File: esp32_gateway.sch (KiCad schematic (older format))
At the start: 75 parts, among them J1 POWER Int, J10 IRF, J11 Conn_01x01_Female, J12 Conn_01x01_Female, J13 Conn_01x01_Female, J14 Conn_01x01_Female, J15 Conn_01x01_Female, J16 Conn_01x01_Female, J17 Conn_01x01_Female, J18 Conn_01x01_Female, J19 Conn_01x01_Female, J2 POWER Out, J20 CC2530_B, J21 CC2530_A, J22 Conn_01x01_Female, J23 Conn_01x01_Female, J3 Conn_01x01_Female, J4 Conn_01x01_Female, J5 Uart, J6 Boot, J7 SRX882, J8 STX882, J9 Conn_01x01_Female, Q1 DMP4051LK3, Q2 BC847, Q3 BSS138, Q4 2N7002, Q5 2N7002, SW1 Reset, U1 LM1117-3.3, U2 ESP32-S

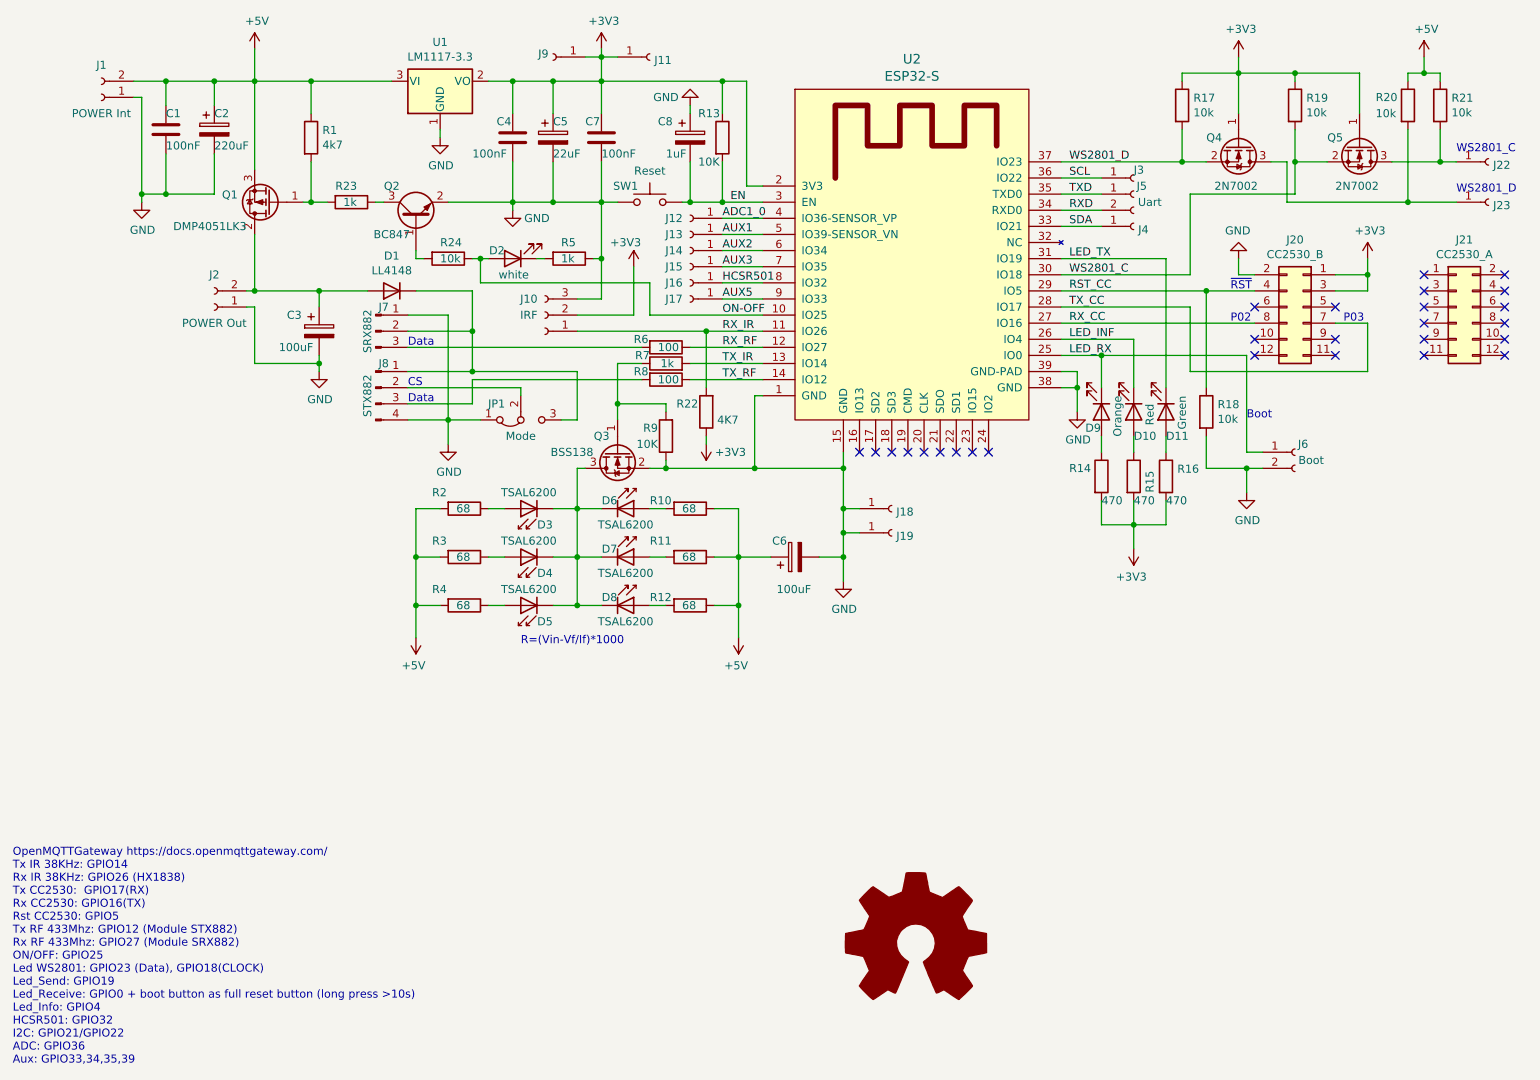
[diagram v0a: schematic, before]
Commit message: Fixed errors in RF modules connection
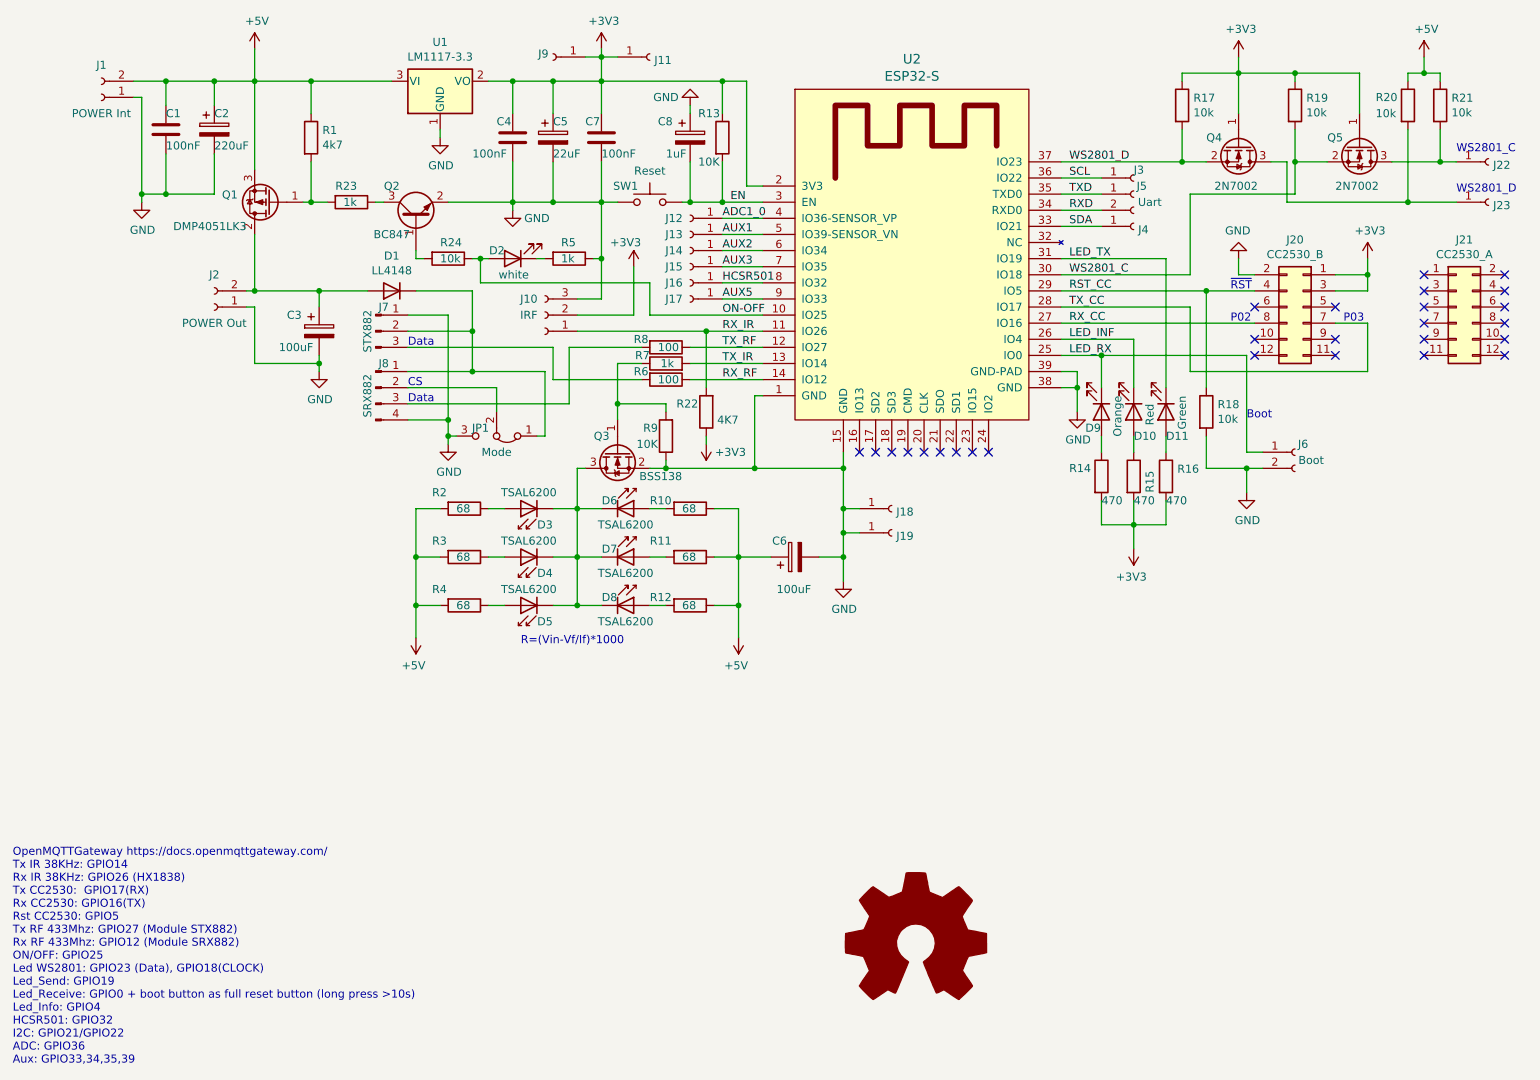
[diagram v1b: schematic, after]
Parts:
- J7: value SRX882 -> STX882
- J8: value STX882 -> SRX882
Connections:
- net GND: now also JP1.3 (B); no longer JP1.1 (A)
- net RX_RF: now also U2.14 (IO12); no longer U2.12 (IO27)
- net TX_RF: now also U2.12 (IO27); no longer U2.14 (IO12)
- net at D1.1 (K), J7.2 (Pin_2), J8.1 (Pin_1): now also JP1.1 (A); no longer JP1.3 (B)
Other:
- note added: "OpenMQTTGateway https://docs.openmqttgateway.com/\nTx IR 38KHz: GPIO14 \nRx IR 38KHz: GPIO26 (HX1838)\nTx CC2530: GPIO17(RX)\nRx CC2530: GPIO16(TX)\nRst CC2530: GPIO5\nTx RF 433Mhz: GPIO27 (Module STX882)\nRx RF 433Mhz: GPIO12 (Module SRX882)\nON/OFF: GPIO25\nLed WS2801: GPIO23 (Data), GPIO18(CLOCK)\nLed_Send: GPIO19\nLed_Receive: GPIO0 + boot button as full reset button (long press >10s)\nLed_In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"
- note removed: "OpenMQTTGateway https://docs.openmqttgateway.com/\nTx IR 38KHz: GPIO14 \nRx IR 38KHz: GPIO26 (HX1838)\nTx CC2530: GPIO17(RX)\nRx CC2530: GPIO16(TX)\nRst CC2530: GPIO5\nTx RF 433Mhz: GPIO12 (Module STX882)\nRx RF 433Mhz: GPIO27 (Module SRX882)\nON/OFF: GPIO25\nLed WS2801: GPIO23 (Data), GPIO18(CLOCK)\nLed_Send: GPIO19\nLed_Receive: GPIO0 + boot button as full reset button (long press >10s)\nLed_In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"
- moved on the sheet: JP1, R6, R8
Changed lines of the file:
@@
 Comment4 ""
 $EndDescr
-Text Notes 600  7750 0    50   ~ 0
-OpenMQTTGateway https://docs.openmqttgateway.com/\nTx IR 38KHz: GPIO14 \nRx IR 38KHz: GPIO26 (HX1838)\nTx CC2530:  GPIO17(RX)\nRx CC2530: GPIO16(TX)\nRst CC2530: GPIO5\nTx RF 433Mhz: GPIO12 (Module STX882)\nRx RF 433Mhz: GPIO27 (Module SRX882)\nON/OFF: GPIO25\nLed WS2801: GPIO23 (Data), GPIO18(CLOCK)\nLed_Send: GPIO19\nLed_Receive: GPIO0 + boot button as full reset button (long press >10s)\nLed_Info: GPIO4\nHCSR501: GPIO32\nI2C: GPIO21/GPIO22\nADC: GPIO36\nAux: GPIO33,34,35,39\n
 NoConn ~ 6450 3950
 NoConn ~ 6350 3950
@@
 RX_CC
 Text Label 5000 3500 0    50   ~ 0
-TX_RF
-Text Label 5000 3300 0    50   ~ 0
 RX_RF
 Text Label 7150 2750 0    50   ~ 0
@@
 $EndComp
 Wire Wire Line
-	3300 3750 3300 3900
+	3300 3750 3300 3850
 Connection ~ 3300 3750
 $Comp
@@
 Connection ~ 9450 2150
 $Comp
-L Device:R R8
-U 1 1 5FBA51B6
+L Device:R R6
+U 1 1 5FBBFD7C
 P 4650 3500
-F 0 "R8" V 4600 3300 50  0000 L CNN
+F 0 "R6" V 4600 3300 50  0000 L CNN
 F 1 "100" V 4650 3450 50  0000 L CNN
 F 2 "Resistor_SMD:R_0805_2012Metric" V 4580 3500 50  0001 C CNN
@@
 	0    1    1    0
 $EndComp
-Wire Wire Line
-	4800 3500 5250 3500
-$Comp
-L Device:R R6
-U 1 1 5FBBFD7C
-P 4650 3300
-F 0 "R6" V 4600 3100 50  0000 L CNN
-F 1 "100" V 4650 3250 50  0000 L CNN
-F 2 "Resistor_SMD:R_0805_2012Metric" V 4580 3300 50  0001 C CNN
-F 3 "~" H 4650 3300 50  0001 C CNN
-	1    4650 3300
-	0    1    1    0
-$EndComp
-Wire Wire Line
-	4800 3300 5250 3300
 Connection ~ 3450 3200
 Wire Wire Line
@@
 CS
 Wire Wire Line
-	3050 3550 3750 3550
-Wire Wire Line
 	3050 3200 3450 3200
 Wire Wire Line
@@
 P 2850 3550
 F 0 "J8" H 2900 3700 50  0000 C CNN
-F 1 "STX882" V 2800 3500 50  0000 C CNN
+F 1 "SRX882" V 2800 3500 50  0000 C CNN
 F 2 "Connector_PinHeader_2.54mm:PinHeader_1x04_P2.54mm_Vertical" H 2850 3550 50  0001 C CNN
 F 3 "~" H 2850 3550 50  0001 C CNN
@@
 	1    0    0    -1
 $EndComp
-Wire Wire Line
-	3050 3300 4500 3300
 $Comp
 L Connector:Conn_01x03_Female J10
@@
 	1    0    0    -1
 $EndComp
-$Comp
-L Jumper:Jumper_3_Bridged12 JP1
-U 1 1 5FA2F7B6
-P 3750 3750
-F 0 "JP1" H 3600 3650 50  0000 C CNN
-F 1 "Mode" H 3750 3850 50  0000 C CNN
-F 2 "Jumper:SolderJumper-3_P1.3mm_Bridged2Bar12_Pad1.0x1.5mm_NumberLabels" H 3750 3750 50  0001 C CNN
-F 3 "~" H 3750 3750 50  0001 C CNN
-	1    3750 3750
-	1    0    0    1
-$EndComp
-Wire Wire Line
-	3500 3750 3300 3750
-Wire Wire Line
-	3750 3600 3750 3550
-Wire Wire Line
-	3450 3450 4100 3450
+Wire Wire Line
+	3450 3450 3900 3450
 Connection ~ 3450 3450
 $Comp
@@
 P 2850 3200
 F 0 "J7" H 2900 3350 50  0000 C CNN
-F 1 "SRX882" V 2800 3200 50  0000 C CNN
+F 1 "STX882" V 2800 3200 50  0000 C CNN
 F 2 "Connector_PinHeader_2.54mm:PinHeader_1x03_P2.54mm_Vertical" H 2850 3200 50  0001 C CNN
 F 3 "~" H 2850 3200 50  0001 C CNN
@@
 	3050 3450 3450 3450
 Wire Wire Line
-	3450 3500 3450 3650
-Wire Wire Line
-	3450 3650 3050 3650
-Wire Wire Line
 	3300 3100 3300 3750
-Wire Wire Line
-	3450 3500 4500 3500
 Wire Wire Line
 	3050 3750 3300 3750
@@
 P 4350 3950
 F 0 "Q3" V 4250 4000 50  0000 L CNN
-F 1 "BSS138" V 4350 4100 50  0000 L CNN
+F 1 "BSS138" V 4500 3550 50  0000 L CNN
 F 2 "Package_TO_SOT_SMD:SOT-23" H 4550 3875 50  0001 L CIN
 F 3 "https://www.onsemi.com/pub/Collateral/BSS138-D.PDF" H 4350 3950 50  0001 L CNN
@@
 	0    -1   1    0
 $EndComp
-Wire Wire Line
-	4000 3750 4100 3750
-Wire Wire Line
-	4100 3750 4100 3450
 $Comp
 L power:GND #PWR0105
@@
 Wire Wire Line
 	4800 1800 4800 1850
+Text Label 5000 3300 0    50   ~ 0
+TX_RF
+Wire Wire Line
+	3050 3300 3950 3300
+Text Notes 600  7750 0    50   ~ 0
+OpenMQTTGateway https://docs.openmqttgateway.com/\nTx IR 38KHz: GPIO14 \nRx IR 38KHz: GPIO26 (HX1838)\nTx CC2530:  GPIO17(RX)\nRx CC2530: GPIO16(TX)\nRst CC2530: GPIO5\nTx RF 433Mhz: GPIO27 (Module STX882)\nRx RF 433Mhz: GPIO12 (Module SRX882)\nON/OFF: GPIO25\nLed WS2801: GPIO23 (Data), GPIO18(CLOCK)\nLed_Send: GPIO19\nLed_Receive: GPIO0 + boot button as full reset button (long press >10s)\nLed_Info: GPIO4\nHCSR501: GPIO32\nI2C: GPIO21/GPIO22\nADC: GPIO36\nAux: GPIO33,34,35,39\n
+Wire Wire Line
+	3050 3550 3600 3550
+Wire Wire Line
+	4500 3500 3950 3500
+Wire Wire Line
+	3950 3500 3950 3300
+Wire Wire Line
+	4800 3500 5250 3500
+Wire Wire Line
+	4050 3300 4050 3650
+Wire Wire Line
+	3850 3850 3900 3850
+Wire Wire Line
+	3350 3850 3300 3850
+Connection ~ 3300 3850
+Wire Wire Line
+	3300 3850 3300 3900
+$Comp
+L Jumper:Jumper_3_Bridged12 JP1
+U 1 1 5FA2F7B6
+P 3600 3850
+F 0 "JP1" H 3700 3800 50  0000 C CNN
+F 1 "Mode" H 3600 3950 50  0000 C CNN
+F 2 "Jumper:SolderJumper-3_P1.3mm_Bridged2Bar12_Pad1.0x1.5mm_NumberLabels" H 3600 3850 50  0001 C CNN
+F 3 "~" H 3600 3850 50  0001 C CNN
+	1    3600 3850
+	-1   0    0    1
+$EndComp
+Wire Wire Line
+	3900 3450 3900 3850
+$Comp
+L Device:R R8
+U 1 1 5FBA51B6
+P 4650 3300
+F 0 "R8" V 4600 3100 50  0000 L CNN
+F 1 "100" V 4650 3250 50  0000 L CNN
+F 2 "Resistor_SMD:R_0805_2012Metric" V 4580 3300 50  0001 C CNN
+F 3 "~" H 4650 3300 50  0001 C CNN
+	1    4650 3300
+	0    1    1    0
+$EndComp
+Wire Wire Line
+	3600 3700 3600 3550
+Wire Wire Line
+	5250 3300 4800 3300
+Wire Wire Line
+	4500 3300 4050 3300
+Wire Wire Line
+	3050 3650 4050 3650
 $EndSCHEMATC
